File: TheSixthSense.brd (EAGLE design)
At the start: 44 x 33.5 mm, 84 parts, among them Q1 IRLML 5203, Q10 Si2302CDS, Q2 PDTC114YT, Q3 Si2302CDS, Q4 Si2302CDS, Q5 Si2302CDS, Q6 Si2302CDS, Q7 Si2302CDS, Q8 Si2302CDS, Q9 Si2302CDS, U1 ATXMEGA32E5-AU, U2 MCP73831, U3 LSM303D, U4 MCP1700T-2502E/TT, U6 KPGA-1602CGC-KA, U7 KPGA-1602CGC-KA

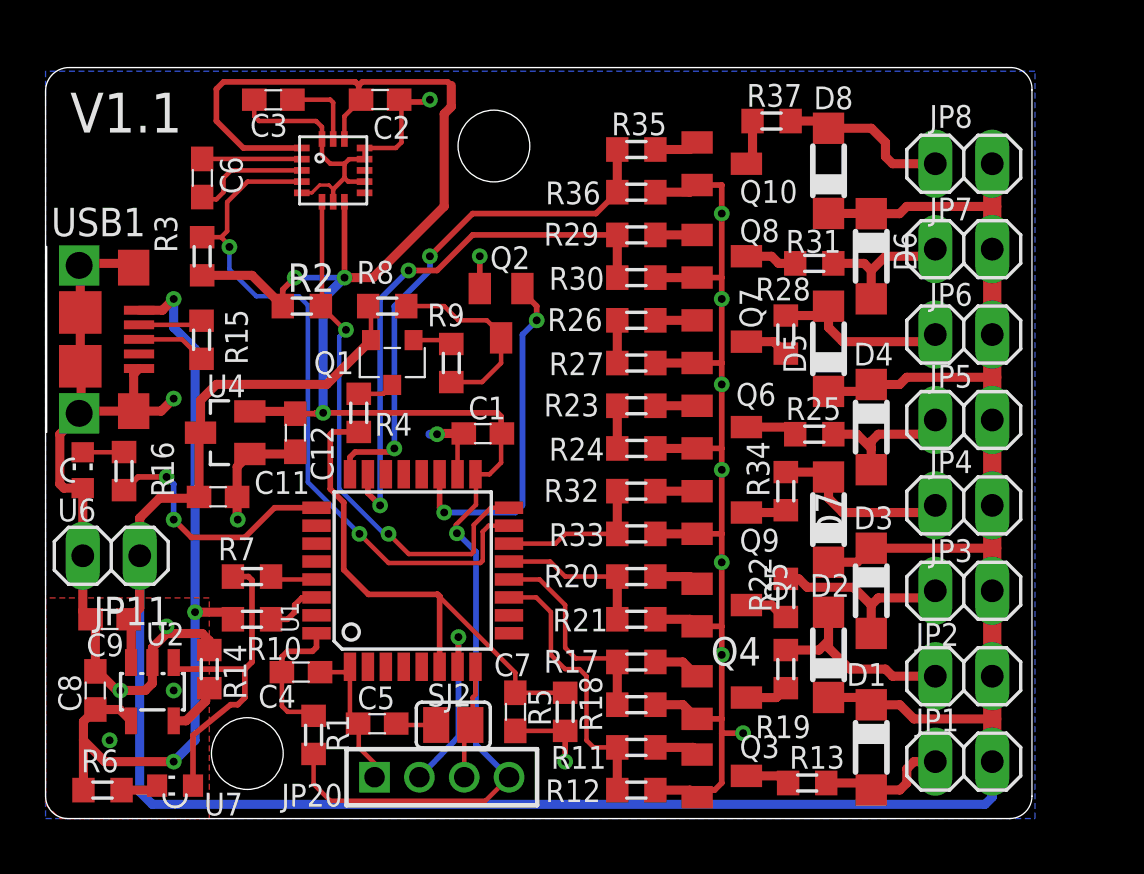
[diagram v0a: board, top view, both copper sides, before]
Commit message: New 8 motor support! - adding motor 5&6: µC <-> Mosfets
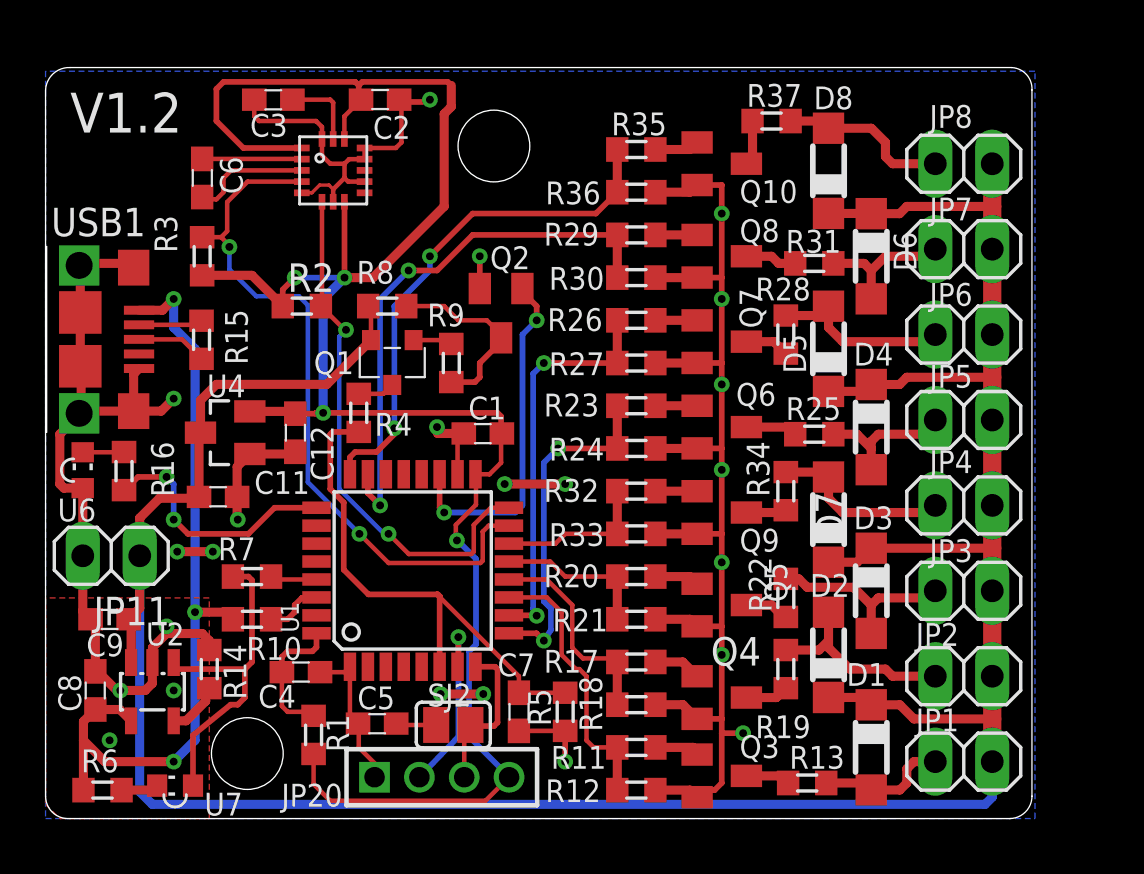
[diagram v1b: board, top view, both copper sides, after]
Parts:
- moved C7 0.16 mm to (21.1, 4.76)
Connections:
- net VIB_MOT_5: now also U1.9
- net VIB_MOT_6: now also U1.10
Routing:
- net VIB_MOT_6: track 1.91 -> 17.9 mm, vias 0 -> 2
- net VIB_MOT_5: track 1.90 -> 15.3 mm, vias 0 -> 2
- net GND: track 127.6 -> 133.5 mm, vias 17 -> 23
- net N$10: track 5.14 -> 7.15 mm
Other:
- board text added: "V1.2"
- board text removed: "V1.1"

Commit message: - new version v1.3 - add a push button - add a fuse - add a switch to disconnect the battery - add a new motor connector
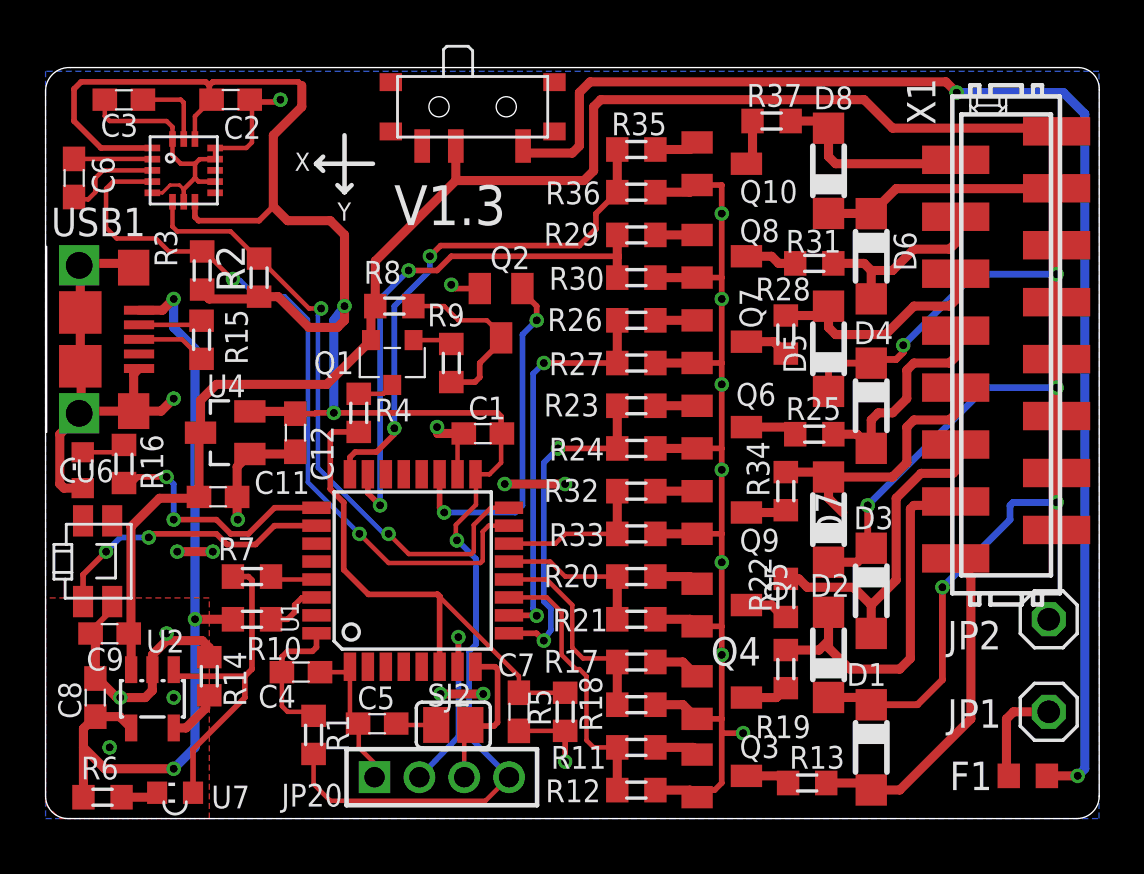
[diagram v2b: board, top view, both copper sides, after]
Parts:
- removed JP11, JP3, JP4, JP5, JP6, JP7, JP8: (no value), pinhead:1X02
- added F1: F0603E0R25FSTR, ptc-littlefuse:R0603
- added S1: ALPSSSSS811101, ALP_Switch:SSSS811101
- added S3: (no value), smd_right_switch:SKSCLAE010
- added X1: MICROMATCH-16SMD, Con-amp-micromatch:MICROMATCH-16SMD
- JP1, JP2: device pinhead:1X02 -> pinhead:1X01
- R14: value 2k -> 4k7
- moved C3 6.67 mm to (3.49, 32.1)
- moved U3 6.67 mm to (6.16, 28.9)
- moved C2 6.67 mm to (8.26, 32.1)
- moved C6 5.71 mm to (1.27, 28.6)
- moved JP2 4.56 mm to (44.7, 8.89), turned to 0 degrees
- moved JP1 4.39 mm to (44.7, 4.76), turned to 0 degrees
- moved R2 2.29 mm to (9.53, 24.1), turned to 90 degrees
- moved D4 0.95 mm to (36.8, 18.4)
- moved C9 0.63 mm to (2.86, 8.26)
- moved R3 0.63 mm to (6.99, 24.4)
- moved R14 0.32 mm to (7.30, 6.35)
- moved R16 0.32 mm to (3.50, 15.8)
- moved R6 0.32 mm to (2.54, 0.95)
- moved C8 0.32 mm to (2.22, 5.40)
- moved U2 0.32 mm to (4.77, 5.34)
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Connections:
- new net N$35: F1.2, JP1.1
- new net N$36: S3.2, U1.26
- new net N$5: F1.1, S1.P1
- net +4.1V: now also S1.P2, X1.1, X1.11, X1.13, X1.15, X1.3, X1.5, X1.7, X1.9; no longer JP1.1, JP11.1, JP2.1, JP3.1, JP4.1, JP5.1, JP6.1, JP7.1, JP8.1
- net GND: now also JP2.1, S3.4; no longer JP11.2
- net N$17: now also X1.16; no longer JP1.2
- net N$21: now also X1.14; no longer JP2.2
- net N$24: now also X1.12; no longer JP3.2
- net N$28: now also X1.8; no longer JP5.2
- net N$31: now also X1.6; no longer JP6.2
- net N$34: now also X1.4; no longer JP7.2
- net N$45: now also X1.10; no longer JP4.2
- net N$48: now also X1.2; no longer JP8.2
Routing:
- net N$5: track 0.00 -> 59.6 mm, vias 0 -> 2
- net N$36: track 0.00 -> 12.9 mm, vias 0 -> 2
- net N$17: track 5.89 -> 15.3 mm
- net N$21: track 8.95 -> 16.7 mm
- net N$24: track 8.68 -> 15.2 mm
- net +4.1V: track 132.2 -> 138.2 mm, vias 0 -> 6
- net N$35: track 0.00 -> 4.87 mm
- net N$45: track 8.10 -> 12.8 mm
- net GND: track 133.5 -> 129.1 mm
- net SDA: track 23.9 -> 28.1 mm
- net N$28: track 6.47 -> 10.3 mm
- net N$31: track 8.18 -> 10.7 mm
- net N$34: track 6.34 -> 8.57 mm
- net SCL: track 31.8 -> 33.8 mm
- net N$48: track 7.62 -> 9.17 mm
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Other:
- board size 44 x 33.5 mm -> 47 x 33.5 mm
- board text added: "Designed by"
- board text added: "Sebastian Förster"
- board text added: "V1.3"
- board text added: "X"
- board text added: "Y"
- board text removed: "V1.2"
